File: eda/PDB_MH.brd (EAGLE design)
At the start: 101.6 x 81.3 mm, 28 parts

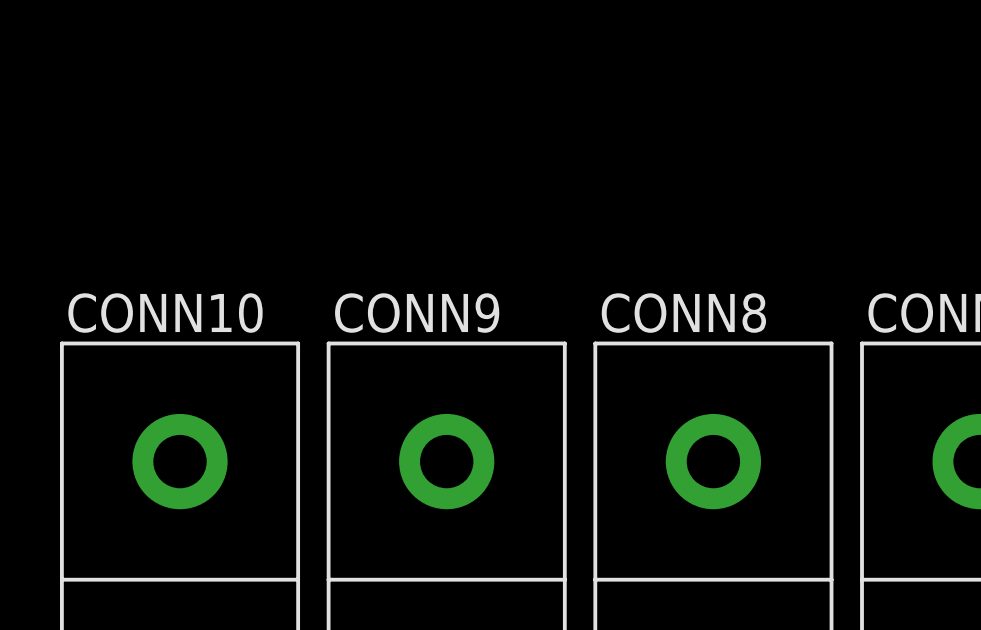
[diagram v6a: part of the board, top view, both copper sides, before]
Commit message: Renamed Wires according to naming conventions
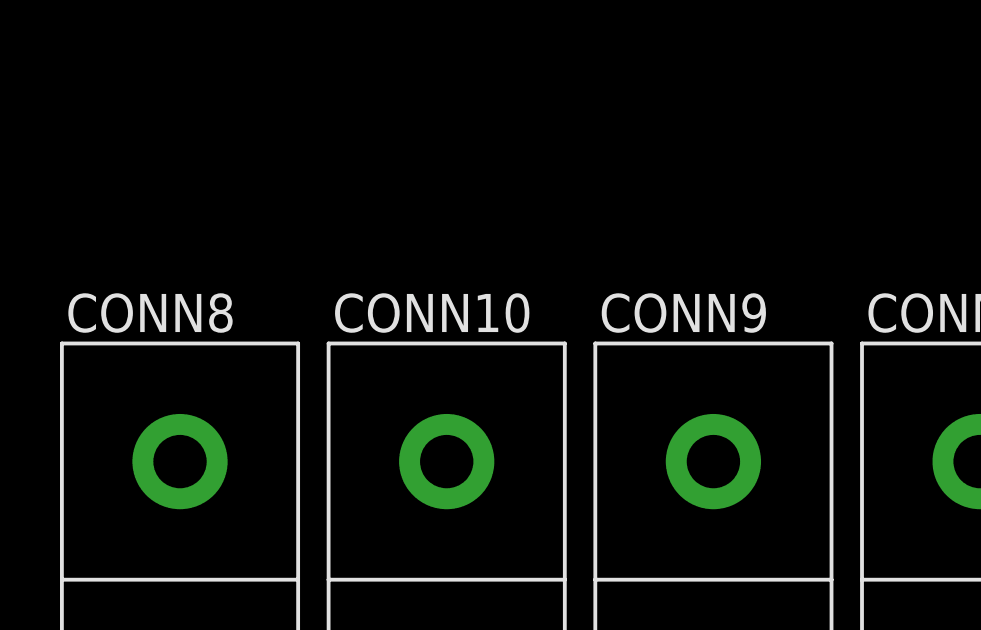
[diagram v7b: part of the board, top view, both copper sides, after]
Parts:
- moved CONN8 17.8 mm to (-31.8, -115.6)
- moved CONN10 8.89 mm to (-22.9, -115.6)
- moved CONN9 8.89 mm to (-14.0, -115.6)
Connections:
- net N$2 renamed VOUT7
- removed net N$1: FUSE10.P$2_DOWN, FUSE10.P$2_UP, FUSE7.P$1_DOWN, FUSE7.P$1_UP, FUSE8.P$2_DOWN, FUSE8.P$2_UP, FUSE9.P$1_DOWN, FUSE9.P$1_UP, U$7.P$6
- removed net N$3: CONN10.PIN2, FUSE8.P$1_DOWN, FUSE8.P$1_UP
- removed net N$4: CONN9.PIN2, FUSE10.P$1_DOWN, FUSE10.P$1_UP
- removed net N$5: CONN8.PIN2, FUSE9.P$2_DOWN, FUSE9.P$2_UP
- new net VOUT10: CONN10.PIN2, FUSE10.P$1_DOWN, FUSE10.P$1_UP
- new net VOUT8: CONN8.PIN2, FUSE8.P$1_DOWN, FUSE8.P$1_UP
- new net VOUT9: CONN9.PIN2, FUSE9.P$2_DOWN, FUSE9.P$2_UP
- net 12V: now also FUSE10.P$2_DOWN, FUSE10.P$2_UP, FUSE7.P$1_DOWN, FUSE7.P$1_UP, FUSE8.P$2_DOWN, FUSE8.P$2_UP, FUSE9.P$1_DOWN, FUSE9.P$1_UP, U$7.P$6
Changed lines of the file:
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@@
 <attribute name="PIE-INT-REF-NUM" value="Anderson" x="-5.08" y="-115.57" size="1.778" layer="27" display="off"/>
 </element>
-<element name="CONN8" library="pie" package="ANDERSON_VERTICAL" value="ANDERSONVERTICAL" x="-13.97" y="-115.57">
+<element name="CONN9" library="pie" package="ANDERSON_VERTICAL" value="ANDERSONVERTICAL" x="-13.97" y="-115.57">
 <attribute name="PIE-INT-REF-NUM" value="Anderson" x="-13.97" y="-115.57" size="1.778" layer="27" display="off"/>
 </element>
-<element name="CONN9" library="pie" package="ANDERSON_VERTICAL" value="ANDERSONVERTICAL" x="-22.86" y="-115.57">
+<element name="CONN10" library="pie" package="ANDERSON_VERTICAL" value="ANDERSONVERTICAL" x="-22.86" y="-115.57">
 <attribute name="PIE-INT-REF-NUM" value="Anderson" x="-22.86" y="-115.57" size="1.778" layer="27" display="off"/>
 </element>
-<element name="CONN10" library="pie" package="ANDERSON_VERTICAL" value="ANDERSONVERTICAL" x="-31.75" y="-115.57">
+<element name="CONN8" library="pie" package="ANDERSON_VERTICAL" value="ANDERSONVERTICAL" x="-31.75" y="-115.57">
 <attribute name="PIE-INT-REF-NUM" value="Anderson" x="-31.75" y="-115.57" size="1.778" layer="27" display="off"/>
 </element>
@@
 <contactref element="CONN5" pad="PIN1"/>
 <contactref element="CONN6" pad="PIN1"/>
+<contactref element="CONN10" pad="PIN1"/>
+<contactref element="CONN8" pad="PIN1"/>
+<contactref element="CONN7" pad="PIN1"/>
 <contactref element="CONN9" pad="PIN1"/>
-<contactref element="CONN10" pad="PIN1"/>
-<contactref element="CONN7" pad="PIN1"/>
-<contactref element="CONN8" pad="PIN1"/>
 <contactref element="U$7" pad="P$3"/>
 <contactref element="U$7" pad="P$5"/>
@@
 <contactref element="FUSE6" pad="P$1_DOWN"/>
 <contactref element="CIRCUIT_BREAKER" pad="P$2"/>
-</signal>
-<signal name="BAT">
-<contactref element="CIRCUIT_BREAKER" pad="P$1"/>
-<contactref element="U$1" pad="12V"/>
-<polygon width="1.1938" layer="1" isolate="1.27" rank="3">
-<vertex x="81.28" y="80.01"/>
-<vertex x="99.06" y="80.01"/>
-<vertex x="99.06" y="2.54"/>
-<vertex x="80.01" y="2.54"/>
-</polygon>
-<contactref element="U$7" pad="P$4"/>
-<wire x1="93.726" y1="16.51" x2="91.186" y2="49.53" width="0" layer="19" extent="1-1"/>
-<wire x1="36.83" y1="-3.81" x2="93.726" y2="16.51" width="0" layer="19" extent="1-1"/>
-</signal>
-<signal name="VOUT6">
-<contactref element="FUSE6" pad="P$2_UP"/>
-<contactref element="FUSE6" pad="P$2_DOWN"/>
-<contactref element="CONN6" pad="PIN2"/>
-<polygon width="1.1938" layer="1" isolate="1.27">
-<vertex x="44.45" y="57.15"/>
-<vertex x="59.69" y="57.15"/>
-<vertex x="59.69" y="74.93"/>
-<vertex x="44.45" y="74.93"/>
-</polygon>
-</signal>
-<signal name="N$1">
 <contactref element="U$7" pad="P$6"/>
 <contactref element="FUSE10" pad="P$2_DOWN"/>
@@
 <contactref element="FUSE7" pad="P$1_UP"/>
 <contactref element="FUSE7" pad="P$1_DOWN"/>
-<wire x1="16.891" y1="-112.395" x2="16.891" y2="-121.285" width="0" layer="19" extent="1-1"/>
-<wire x1="3.429" y1="-106.045" x2="16.891" y2="-112.395" width="0" layer="19" extent="1-1"/>
-<wire x1="3.429" y1="-97.155" x2="3.429" y2="-106.045" width="0" layer="19" extent="1-1"/>
-<wire x1="16.891" y1="-90.805" x2="3.429" y2="-97.155" width="0" layer="19" extent="1-1"/>
-<wire x1="16.891" y1="-81.915" x2="16.891" y2="-90.805" width="0" layer="19" extent="1-1"/>
-<wire x1="3.429" y1="-75.565" x2="16.891" y2="-81.915" width="0" layer="19" extent="1-1"/>
-<wire x1="3.429" y1="-66.675" x2="3.429" y2="-75.565" width="0" layer="19" extent="1-1"/>
-<wire x1="25.4" y1="-3.81" x2="3.429" y2="-66.675" width="0" layer="19" extent="1-1"/>
-</signal>
-<signal name="N$2">
+<wire x1="56.515" y1="46.609" x2="73.914" y2="49.53" width="0" layer="19" extent="1-1"/>
+<wire x1="47.625" y1="46.609" x2="56.515" y2="46.609" width="0" layer="19" extent="1-1"/>
+<wire x1="38.735" y1="46.609" x2="47.625" y2="46.609" width="0" layer="19" extent="1-1"/>
+<wire x1="29.845" y1="46.609" x2="38.735" y2="46.609" width="0" layer="19" extent="1-1"/>
+<wire x1="20.955" y1="46.609" x2="29.845" y2="46.609" width="0" layer="19" extent="1-1"/>
+<wire x1="12.065" y1="46.609" x2="20.955" y2="46.609" width="0" layer="19" extent="1-1"/>
+<wire x1="56.515" y1="35.941" x2="56.515" y2="46.609" width="0" layer="19" extent="1-1"/>
+<wire x1="47.625" y1="35.941" x2="56.515" y2="35.941" width="0" layer="19" extent="1-1"/>
+<wire x1="38.735" y1="35.941" x2="47.625" y2="35.941" width="0" layer="19" extent="1-1"/>
+<wire x1="29.845" y1="35.941" x2="38.735" y2="35.941" width="0" layer="19" extent="1-1"/>
+<wire x1="20.955" y1="35.941" x2="29.845" y2="35.941" width="0" layer="19" extent="1-1"/>
+<wire x1="12.065" y1="35.941" x2="20.955" y2="35.941" width="0" layer="19" extent="1-1"/>
+<wire x1="25.4" y1="-3.81" x2="29.845" y2="35.941" width="0" layer="19" extent="1-1"/>
+<wire x1="3.429" y1="-66.675" x2="25.4" y2="-3.81" width="0" layer="19" extent="1-1"/>
+<wire x1="3.429" y1="-75.565" x2="3.429" y2="-66.675" width="0" layer="19" extent="1-1"/>
+<wire x1="16.891" y1="-81.915" x2="3.429" y2="-75.565" width="0" layer="19" extent="1-1"/>
+<wire x1="16.891" y1="-90.805" x2="16.891" y2="-81.915" width="0" layer="19" extent="1-1"/>
+<wire x1="3.429" y1="-97.155" x2="16.891" y2="-90.805" width="0" layer="19" extent="1-1"/>
+<wire x1="3.429" y1="-106.045" x2="3.429" y2="-97.155" width="0" layer="19" extent="1-1"/>
+<wire x1="16.891" y1="-112.395" x2="3.429" y2="-106.045" width="0" layer="19" extent="1-1"/>
+<wire x1="16.891" y1="-121.285" x2="16.891" y2="-112.395" width="0" layer="19" extent="1-1"/>
+</signal>
+<signal name="BAT">
+<contactref element="CIRCUIT_BREAKER" pad="P$1"/>
+<contactref element="U$1" pad="12V"/>
+<polygon width="1.1938" layer="1" isolate="1.27" rank="3">
+<vertex x="81.28" y="80.01"/>
+<vertex x="99.06" y="80.01"/>
+<vertex x="99.06" y="2.54"/>
+<vertex x="80.01" y="2.54"/>
+</polygon>
+<contactref element="U$7" pad="P$4"/>
+<wire x1="93.726" y1="16.51" x2="91.186" y2="49.53" width="0" layer="19" extent="1-1"/>
+<wire x1="36.83" y1="-3.81" x2="93.726" y2="16.51" width="0" layer="19" extent="1-1"/>
+</signal>
+<signal name="VOUT6">
+<contactref element="FUSE6" pad="P$2_UP"/>
+<contactref element="FUSE6" pad="P$2_DOWN"/>
+<contactref element="CONN6" pad="PIN2"/>
+<polygon width="1.1938" layer="1" isolate="1.27">
+<vertex x="44.45" y="57.15"/>
+<vertex x="59.69" y="57.15"/>
+<vertex x="59.69" y="74.93"/>
+<vertex x="44.45" y="74.93"/>
+</polygon>
+</signal>
+<signal name="VOUT7">
 <contactref element="FUSE7" pad="P$2_DOWN"/>
 <contactref element="FUSE7" pad="P$2_UP"/>
@@
 <wire x1="16.891" y1="-66.675" x2="16.891" y2="-75.565" width="0" layer="19" extent="1-1"/>
 </signal>
-<signal name="N$3">
+<signal name="VOUT8">
 <contactref element="FUSE8" pad="P$1_UP"/>
 <contactref element="FUSE8" pad="P$1_DOWN"/>
-<contactref element="CONN10" pad="PIN2"/>
+<contactref element="CONN8" pad="PIN2"/>
 <wire x1="3.429" y1="-90.805" x2="-31.75" y2="-111.633" width="0" layer="19" extent="1-1"/>
 <wire x1="3.429" y1="-81.915" x2="3.429" y2="-90.805" width="0" layer="19" extent="1-1"/>
 </signal>
-<signal name="N$5">
+<signal name="VOUT9">
 <contactref element="FUSE9" pad="P$2_DOWN"/>
 <contactref element="FUSE9" pad="P$2_UP"/>
-<contactref element="CONN8" pad="PIN2"/>
+<contactref element="CONN9" pad="PIN2"/>
 <wire x1="16.891" y1="-106.045" x2="-13.97" y2="-111.633" width="0" layer="19" extent="1-1"/>
 <wire x1="16.891" y1="-97.155" x2="16.891" y2="-106.045" width="0" layer="19" extent="1-1"/>
 </signal>
-<signal name="N$4">
+<signal name="VOUT10">
 <contactref element="FUSE10" pad="P$1_UP"/>
 <contactref element="FUSE10" pad="P$1_DOWN"/>
-<contactref element="CONN9" pad="PIN2"/>
+<contactref element="CONN10" pad="PIN2"/>
 <wire x1="3.429" y1="-112.395" x2="-22.86" y2="-111.633" width="0" layer="19" extent="1-1"/>
 <wire x1="3.429" y1="-121.285" x2="3.429" y2="-112.395" width="0" layer="19" extent="1-1"/>

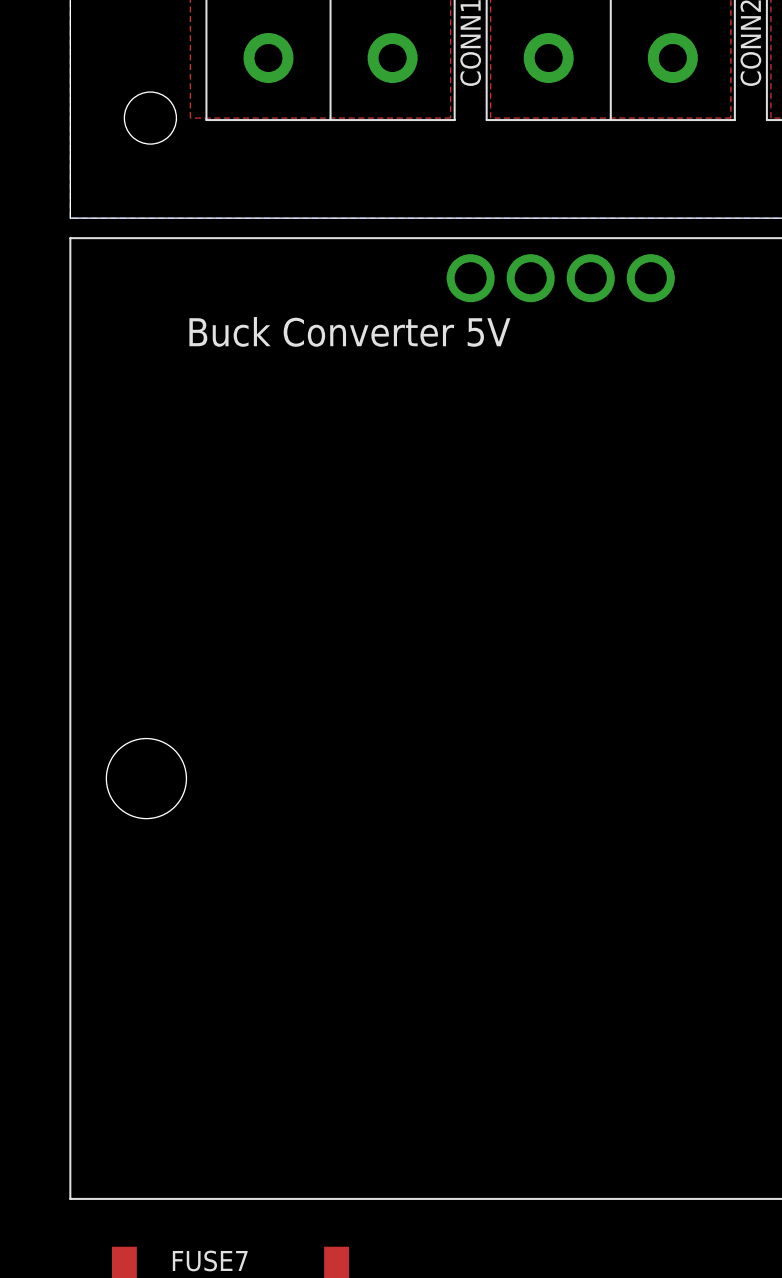
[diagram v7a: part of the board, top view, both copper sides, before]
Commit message: Fix net names and reorganize PDB_MH.sch; add label to buck regulator symbol
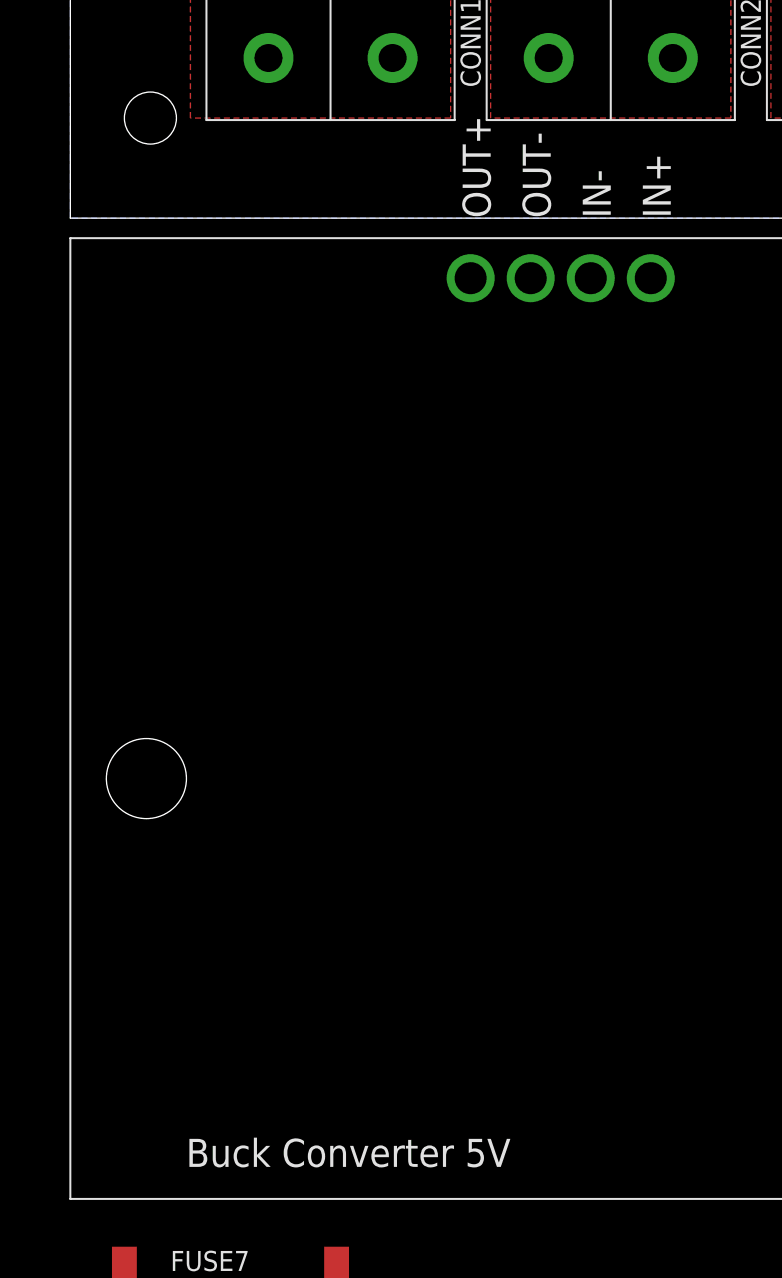
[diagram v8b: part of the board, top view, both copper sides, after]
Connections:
- new net 5V: FUSE10.P$2_DOWN, FUSE10.P$2_UP, FUSE7.P$1_DOWN, FUSE7.P$1_UP, FUSE8.P$2_DOWN, FUSE8.P$2_UP, FUSE9.P$1_DOWN, FUSE9.P$1_UP, U$7.OUT+
- net 12V: no longer FUSE10.P$2_DOWN, FUSE10.P$2_UP, FUSE7.P$1_DOWN, FUSE7.P$1_UP, FUSE8.P$2_DOWN, FUSE8.P$2_UP, FUSE9.P$1_DOWN, FUSE9.P$1_UP, U$7.P$6
- net BAT: now also U$7.IN+; no longer U$7.P$4
- net GND: now also U$7.IN-, U$7.OUT-; no longer U$7.P$3, U$7.P$5
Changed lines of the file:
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@@
 <?xml version="1.0" encoding="utf-8"?>
 <!DOCTYPE eagle SYSTEM "eagle.dtd">
-<eagle version="7.6.0">
+<eagle version="7.4.0">
 <drawing>
 <settings>
@@
 <contactref element="CONN7" pad="PIN1"/>
 <contactref element="CONN9" pad="PIN1"/>
-<contactref element="U$7" pad="P$3"/>
-<contactref element="U$7" pad="P$5"/>
+<contactref element="U$7" pad="IN-"/>
+<contactref element="U$7" pad="OUT-"/>
 <wire x1="-22.86" y1="-119.507" x2="-31.75" y2="-119.507" width="0" layer="19" extent="1-1"/>
 <wire x1="-13.97" y1="-119.507" x2="-22.86" y2="-119.507" width="0" layer="19" extent="1-1"/>
@@
 <contactref element="FUSE6" pad="P$1_DOWN"/>
 <contactref element="CIRCUIT_BREAKER" pad="P$2"/>
-<contactref element="U$7" pad="P$6"/>
-<contactref element="FUSE10" pad="P$2_DOWN"/>
-<contactref element="FUSE10" pad="P$2_UP"/>
-<contactref element="FUSE9" pad="P$1_UP"/>
-<contactref element="FUSE9" pad="P$1_DOWN"/>
-<contactref element="FUSE8" pad="P$2_DOWN"/>
-<contactref element="FUSE8" pad="P$2_UP"/>
-<contactref element="FUSE7" pad="P$1_UP"/>
-<contactref element="FUSE7" pad="P$1_DOWN"/>
 <wire x1="56.515" y1="46.609" x2="73.914" y2="49.53" width="0" layer="19" extent="1-1"/>
 <wire x1="47.625" y1="46.609" x2="56.515" y2="46.609" width="0" layer="19" extent="1-1"/>
@@
 <wire x1="20.955" y1="35.941" x2="29.845" y2="35.941" width="0" layer="19" extent="1-1"/>
 <wire x1="12.065" y1="35.941" x2="20.955" y2="35.941" width="0" layer="19" extent="1-1"/>
-<wire x1="25.4" y1="-3.81" x2="29.845" y2="35.941" width="0" layer="19" extent="1-1"/>
-<wire x1="3.429" y1="-66.675" x2="25.4" y2="-3.81" width="0" layer="19" extent="1-1"/>
-<wire x1="3.429" y1="-75.565" x2="3.429" y2="-66.675" width="0" layer="19" extent="1-1"/>
-<wire x1="16.891" y1="-81.915" x2="3.429" y2="-75.565" width="0" layer="19" extent="1-1"/>
-<wire x1="16.891" y1="-90.805" x2="16.891" y2="-81.915" width="0" layer="19" extent="1-1"/>
-<wire x1="3.429" y1="-97.155" x2="16.891" y2="-90.805" width="0" layer="19" extent="1-1"/>
-<wire x1="3.429" y1="-106.045" x2="3.429" y2="-97.155" width="0" layer="19" extent="1-1"/>
-<wire x1="16.891" y1="-112.395" x2="3.429" y2="-106.045" width="0" layer="19" extent="1-1"/>
-<wire x1="16.891" y1="-121.285" x2="16.891" y2="-112.395" width="0" layer="19" extent="1-1"/>
 </signal>
 <signal name="BAT">
@@
 <vertex x="80.01" y="2.54"/>
 </polygon>
-<contactref element="U$7" pad="P$4"/>
+<contactref element="U$7" pad="IN+"/>
 <wire x1="93.726" y1="16.51" x2="91.186" y2="49.53" width="0" layer="19" extent="1-1"/>
 <wire x1="36.83" y1="-3.81" x2="93.726" y2="16.51" width="0" layer="19" extent="1-1"/>
@@
 <wire x1="3.429" y1="-121.285" x2="3.429" y2="-112.395" width="0" layer="19" extent="1-1"/>
 </signal>
+<signal name="5V">
+<contactref element="U$7" pad="OUT+"/>
+<contactref element="FUSE10" pad="P$2_UP"/>
+<contactref element="FUSE10" pad="P$2_DOWN"/>
+<contactref element="FUSE9" pad="P$1_UP"/>
+<contactref element="FUSE9" pad="P$1_DOWN"/>
+<contactref element="FUSE8" pad="P$2_UP"/>
+<contactref element="FUSE8" pad="P$2_DOWN"/>
+<contactref element="FUSE7" pad="P$1_UP"/>
+<contactref element="FUSE7" pad="P$1_DOWN"/>
+<wire x1="16.891" y1="-112.395" x2="16.891" y2="-121.285" width="0" layer="19" extent="1-1"/>
+<wire x1="3.429" y1="-106.045" x2="16.891" y2="-112.395" width="0" layer="19" extent="1-1"/>
+<wire x1="3.429" y1="-97.155" x2="3.429" y2="-106.045" width="0" layer="19" extent="1-1"/>
+<wire x1="16.891" y1="-90.805" x2="3.429" y2="-97.155" width="0" layer="19" extent="1-1"/>
+<wire x1="16.891" y1="-81.915" x2="16.891" y2="-90.805" width="0" layer="19" extent="1-1"/>
+<wire x1="3.429" y1="-75.565" x2="16.891" y2="-81.915" width="0" layer="19" extent="1-1"/>
+<wire x1="3.429" y1="-66.675" x2="3.429" y2="-75.565" width="0" layer="19" extent="1-1"/>
+<wire x1="25.4" y1="-3.81" x2="3.429" y2="-66.675" width="0" layer="19" extent="1-1"/>
+</signal>
 </signals>
